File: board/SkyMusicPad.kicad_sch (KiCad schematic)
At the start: 36 parts, among them SW1 Cherry, SW10 Cherry, SW11 Cherry, SW12 Cherry, SW13 Cherry, SW14 Cherry, SW15 Cherry, SW16 RotaryEncoder_Switch, SW2 Cherry, SW3 Cherry, SW4 Cherry, SW5 Cherry, SW6 Cherry, SW7 Cherry, SW8 Cherry, SW9 Cherry

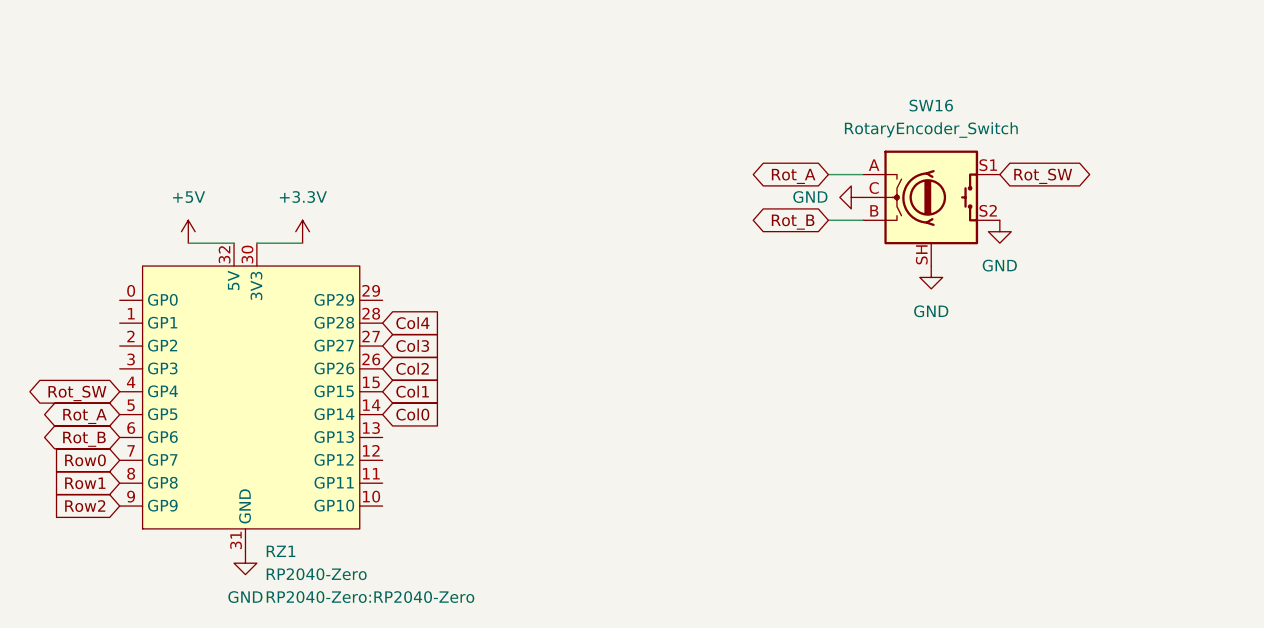
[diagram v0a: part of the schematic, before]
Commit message: Change global net shapes, move encoder position
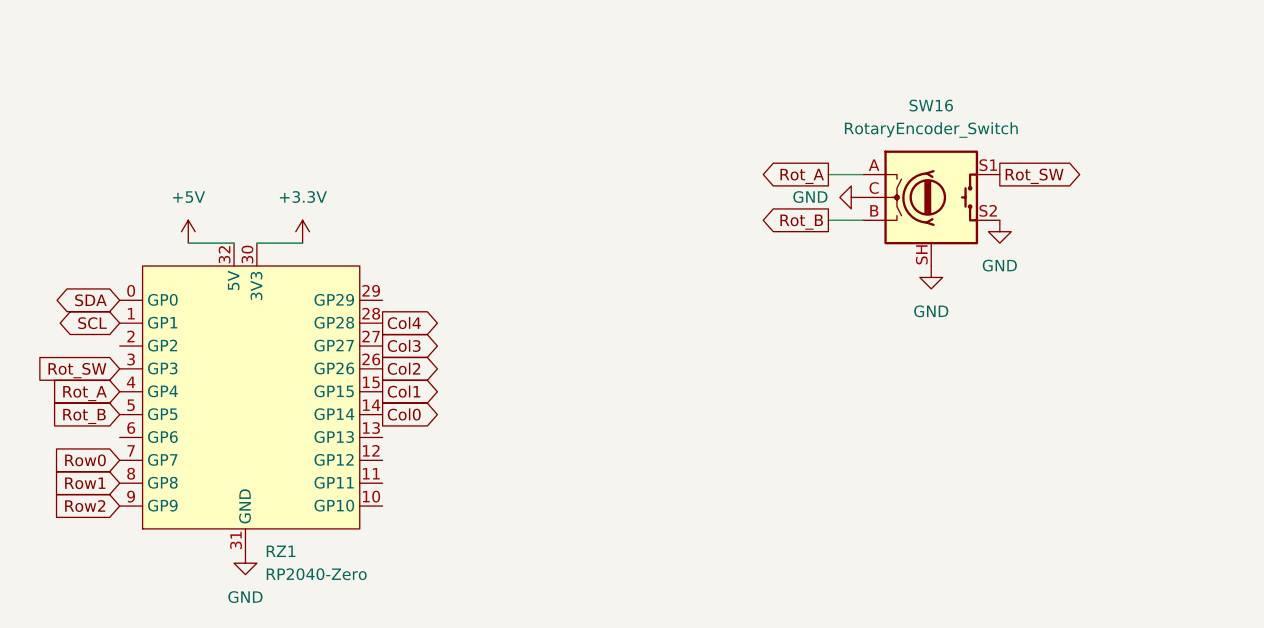
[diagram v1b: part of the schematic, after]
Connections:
- net Rot_A: now also RZ1.4 (GP4); no longer RZ1.5 (GP5)
- net Rot_B: now also RZ1.5 (GP5); no longer RZ1.6 (GP6)
- net Rot_SW: now also RZ1.3 (GP3); no longer RZ1.4 (GP4)
- net SDA: now reaches RZ1.0 (GP0)
- net SCL: now reaches RZ1.1 (GP1)
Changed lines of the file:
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@@
 (kicad_sch
-	(version 20240101)
+	(version 20231120)
 	(generator "eeschema")
-	(generator_version "8.99")
+	(generator_version "8.0")
 	(paper "A4")
 	(junction
@@
 		)
 	)
+	(global_label "SCL"
+		(shape bidirectional)
+		(at 52.07 133.35 180)
+		(fields_autoplaced yes)
+		(effects
+			(font
+				(size 1.27 1.27)
+			)
+			(justify right)
+		)
+		(property "Intersheetrefs" "${INTERSHEET_REFS}"
+			(at 44.4659 133.35 0)
+			(effects
+				(font
+					(size 1.27 1.27)
+				)
+				(justify right)
+				(hide yes)
+			)
+		)
+	)
 	(global_label "Row2"
 		(shape input)
@@
 	)
 	(global_label "Col1"
-		(shape input)
+		(shape output)
 		(at 81.28 140.97 0)
 		(fields_autoplaced yes)
@@
 	)
 	(global_label "Rot_A"
-		(shape bidirectional)
+		(shape output)
 		(at 130.81 116.84 180)
 		(fields_autoplaced yes)
@@
 		)
 		(property "Intersheetrefs" "${INTERSHEET_REFS}"
-			(at 121.5126 116.84 0)
+			(at 122.6239 116.84 0)
 			(effects
 				(font
@@
 	)
 	(global_label "Rot_B"
-		(shape bidirectional)
-		(at 52.07 146.05 180)
+		(shape input)
+		(at 52.07 143.51 180)
 		(fields_autoplaced yes)
 		(effects
@@
 		)
 		(property "Intersheetrefs" "${INTERSHEET_REFS}"
-			(at 42.5912 146.05 0)
+			(at 43.7025 143.51 0)
 			(effects
 				(font
@@
 	)
 	(global_label "Col2"
-		(shape input)
+		(shape output)
 		(at 81.28 138.43 0)
 		(fields_autoplaced yes)
@@
 	)
 	(global_label "Rot_SW"
-		(shape bidirectional)
-		(at 52.07 140.97 180)
+		(shape input)
+		(at 52.07 138.43 180)
 		(fields_autoplaced yes)
 		(effects
@@
 		)
 		(property "Intersheetrefs" "${INTERSHEET_REFS}"
-			(at 41.2003 140.97 0)
+			(at 42.3116 138.43 0)
 			(effects
 				(font
@@
 	)
 	(global_label "Col0"
-		(shape input)
+		(shape output)
 		(at 81.28 143.51 0)
 		(fields_autoplaced yes)
@@
 	)
 	(global_label "Rot_A"
-		(shape bidirectional)
-		(at 52.07 143.51 180)
+		(shape input)
+		(at 52.07 140.97 180)
 		(fields_autoplaced yes)
 		(effects
@@
 		)
 		(property "Intersheetrefs" "${INTERSHEET_REFS}"
-			(at 42.7726 143.51 0)
+			(at 43.8839 140.97 0)
 			(effects
 				(font
@@
 	)
 	(global_label "Col4"
-		(shape input)
+		(shape output)
 		(at 81.28 133.35 0)
 		(fields_autoplaced yes)
@@
 		)
 	)
+	(global_label "SDA"
+		(shape bidirectional)
+		(at 52.07 130.81 180)
+		(fields_autoplaced yes)
+		(effects
+			(font
+				(size 1.27 1.27)
+			)
+			(justify right)
+		)
+		(property "Intersheetrefs" "${INTERSHEET_REFS}"
+			(at 44.4054 130.81 0)
+			(effects
+				(font
+					(size 1.27 1.27)
+				)
+				(justify right)
+				(hide yes)
+			)
+		)
+	)
 	(global_label "Col1"
 		(shape input)
@@
 	)
 	(global_label "Col3"
-		(shape input)
+		(shape output)
 		(at 81.28 135.89 0)
 		(fields_autoplaced yes)
@@
 	)
 	(global_label "Rot_SW"
-		(shape bidirectional)
+		(shape output)
 		(at 149.86 116.84 0)
 		(fields_autoplaced yes)
@@
 		)
 		(property "Intersheetrefs" "${INTERSHEET_REFS}"
-			(at 160.7297 116.84 0)
+			(at 159.6184 116.84 0)
 			(effects
 				(font
@@
 	)
 	(global_label "Rot_B"
-		(shape bidirectional)
+		(shape output)
 		(at 130.81 121.92 180)
 		(fields_autoplaced yes)
@@
 		)
 		(property "Intersheetrefs" "${INTERSHEET_REFS}"
-			(at 121.3312 121.92 0)
+			(at 122.4425 121.92 0)
 			(effects
 				(font
@@
 				)
 				(justify left)
+				(hide yes)
 			)
 		)

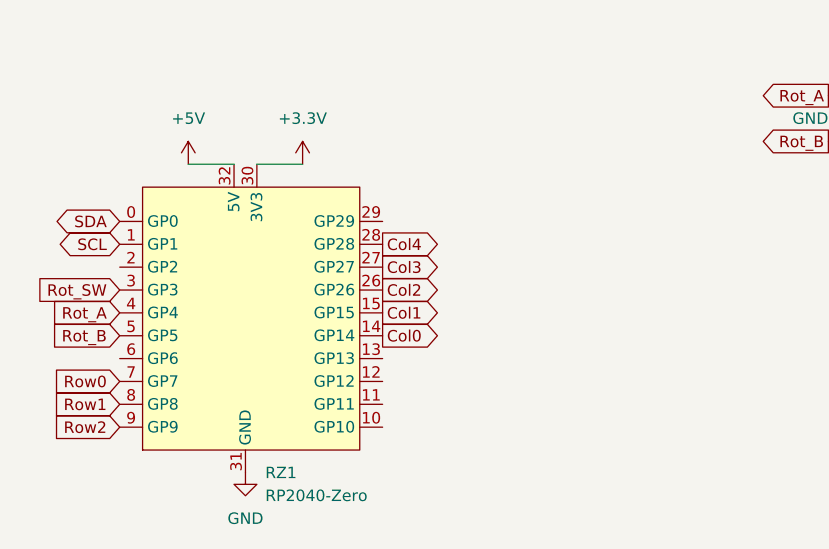
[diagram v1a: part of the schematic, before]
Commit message: Code migration
- Remove CircuitPython code
- Begin Arduino code development
- Add patched BLE Keyboard library
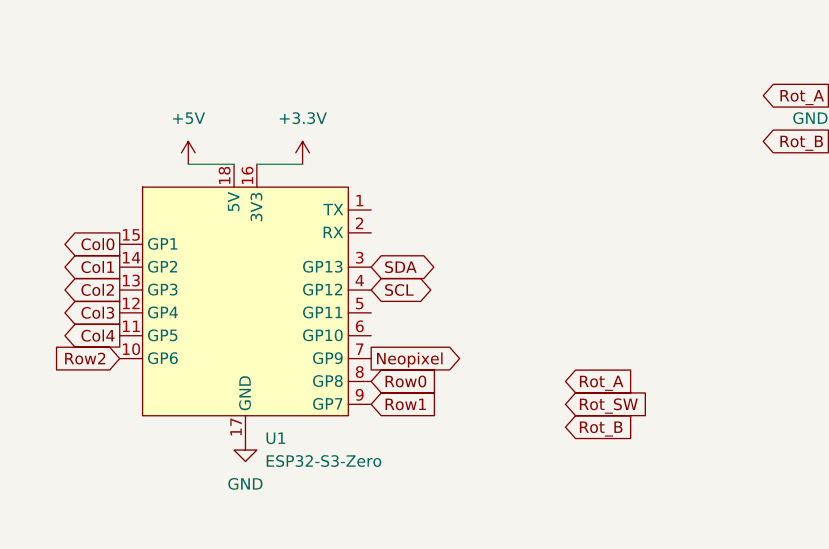
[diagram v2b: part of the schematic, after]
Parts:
- removed RZ1: RP2040-Zero, RP2040-Zero:RP2040-Zero, symbol rp2040-zero:RP2040-Zero
- added U1: ESP32-S3-Zero, ESP32-S3-Zero:ESP32-S3-Zero, symbol ESP32-S3-Zero:ESP32-S3-Zero
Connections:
- net +3.3V: now also U1.16 (3V3)
- net +5V: now also U1.18 (5V)
- net Col0: now also U1.15 (GP1)
- net Col1: now also U1.14 (GP2)
- net Col2: now also U1.13 (GP3)
- net Col3: now also U1.12 (GP4)
- net Col4: now also U1.11 (GP5)
- net GND: now also U1.17 (GND)
- net Row0: now also U1.8 (GP8)
- net Row1: now also U1.9 (GP7)
- net Row2: now also U1.10 (GP6)
- net SCL: now also U1.4 (GP12)
- net SDA: now also U1.3 (GP13)
- new net Neopixel: U1.7 (GP9)

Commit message: Code and PCB updates
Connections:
- net Rot_A: now also U1.5 (GP11)
- net Rot_B: now also U1.6 (GP10)
- net Rot_SW: now also U1.2 (RX)
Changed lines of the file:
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@@
 	(global_label "Rot_B"
 		(shape input)
-		(at 101.6 153.67 0)
-		(fields_autoplaced yes)
-		(effects
-			(font
-				(size 1.27 1.27)
-			)
-			(justify left)
-		)
-		(property "Intersheetrefs" "${INTERSHEET_REFS}"
-			(at 109.9675 153.67 0)
+		(at 80.01 143.51 0)
+		(fields_autoplaced yes)
+		(effects
+			(font
+				(size 1.27 1.27)
+			)
+			(justify left)
+		)
+		(property "Intersheetrefs" "${INTERSHEET_REFS}"
+			(at 88.3775 143.51 0)
 			(effects
 				(font
@@
 	(global_label "Rot_SW"
 		(shape input)
-		(at 101.6 151.13 0)
-		(fields_autoplaced yes)
-		(effects
-			(font
-				(size 1.27 1.27)
-			)
-			(justify left)
-		)
-		(property "Intersheetrefs" "${INTERSHEET_REFS}"
-			(at 111.3584 151.13 0)
+		(at 80.01 132.08 0)
+		(fields_autoplaced yes)
+		(effects
+			(font
+				(size 1.27 1.27)
+			)
+			(justify left)
+		)
+		(property "Intersheetrefs" "${INTERSHEET_REFS}"
+			(at 89.7684 132.08 0)
 			(effects
 				(font
@@
 	(global_label "Rot_A"
 		(shape input)
-		(at 101.6 148.59 0)
-		(fields_autoplaced yes)
-		(effects
-			(font
-				(size 1.27 1.27)
-			)
-			(justify left)
-		)
-		(property "Intersheetrefs" "${INTERSHEET_REFS}"
-			(at 109.7861 148.59 0)
-			(effects
-				(font
+		(at 80.01 140.97 0)
+		(fields_autoplaced yes)
+		(effects
+			(font
+				(size 1.27 1.27)
+			)
+			(justify left)
+		)
+		(property "Intersheetrefs" "${INTERSHEET_REFS}"
+			(at 88.1961 140.97 0)
+			(effects
+				(font

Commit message: Further board and code development.
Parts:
- added BT1: Battery_Cell, symbol Device:Battery_Cell
- added D16, D17, D18, D19, D20, D21, D22, D23, D24, D25, D26, D27, D28, D29, D30: WS2812B-2020, LED_SMD:LED_WS2812B-2020_PLCC4_2.0x2.0mm, symbol LED:WS2812B-2020
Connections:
- net +3.3V: now also D16.4 (VDD), D17.4 (VDD), D18.4 (VDD), D19.4 (VDD), D20.4 (VDD), D21.4 (VDD), D22.4 (VDD), D23.4 (VDD), D24.4 (VDD), D25.4 (VDD), D26.4 (VDD), D27.4 (VDD), D28.4 (VDD), D29.4 (VDD), D30.4 (VDD)
- net Col0: now also U1.11 (GP5); no longer U1.15 (GP1)
- net Col1: now also U1.12 (GP4); no longer U1.14 (GP2)
- net Col3: now also U1.14 (GP2); no longer U1.12 (GP4)
- net Col4: now also U1.15 (GP1); no longer U1.11 (GP5)
- net GND: now also BT1.2 (-), D16.2 (VSS), D17.2 (VSS), D18.2 (VSS), D19.2 (VSS), D20.2 (VSS), D21.2 (VSS), D22.2 (VSS), D23.2 (VSS), D24.2 (VSS), D25.2 (VSS), D26.2 (VSS), D27.2 (VSS), D28.2 (VSS), D29.2 (VSS), D30.2 (VSS)
- net Neopixel: now also D16.3 (DIN)
- net Batt: now reaches U1.1 (TX)
- net Batt: now also BT1.1 (+)
- new net: D16.1 (DOUT), D17.3 (DIN)
- new net: D27.1 (DOUT), D28.3 (DIN)
- new net: D26.1 (DOUT), D27.3 (DIN)
- new net: D18.1 (DOUT), D19.3 (DIN)
- new net: D17.1 (DOUT), D18.3 (DIN)
- new net: D22.1 (DOUT), D23.3 (DIN)
- new net: D21.1 (DOUT), D22.3 (DIN)
- new net: D29.1 (DOUT), D30.3 (DIN)
- new net: D24.1 (DOUT), D25.3 (DIN)
- new net: D23.1 (DOUT), D24.3 (DIN)
- new net: D28.1 (DOUT), D29.3 (DIN)
- new net: D19.1 (DOUT), D20.3 (DIN)
- new net Row0_out: D20.1 (DOUT), D21.3 (DIN)
- new net Row1_out: D25.1 (DOUT), D26.3 (DIN)

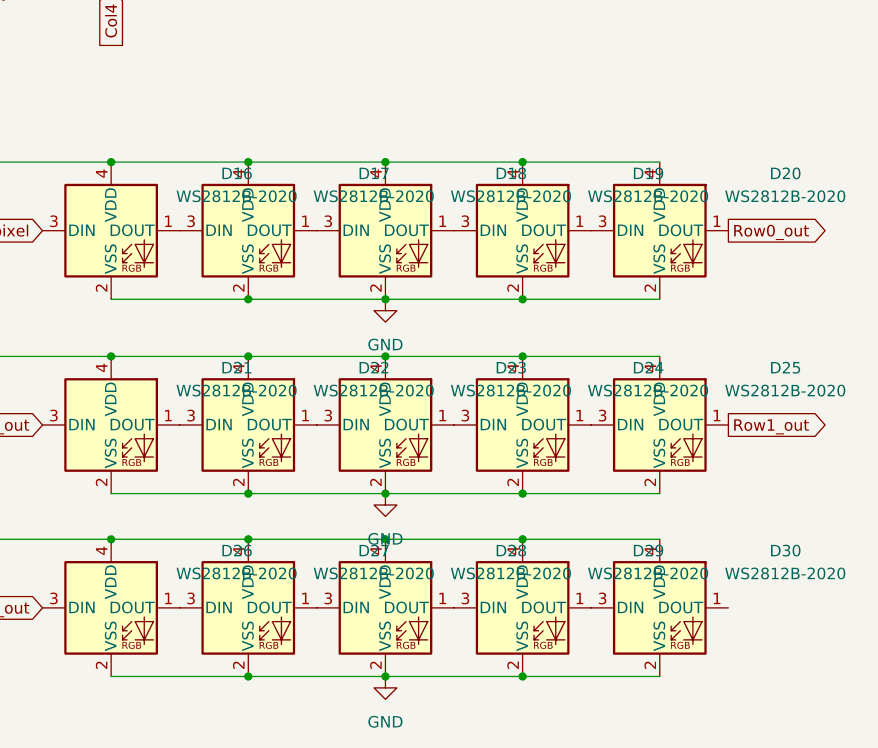
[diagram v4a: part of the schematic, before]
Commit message: Fix and add LEDs
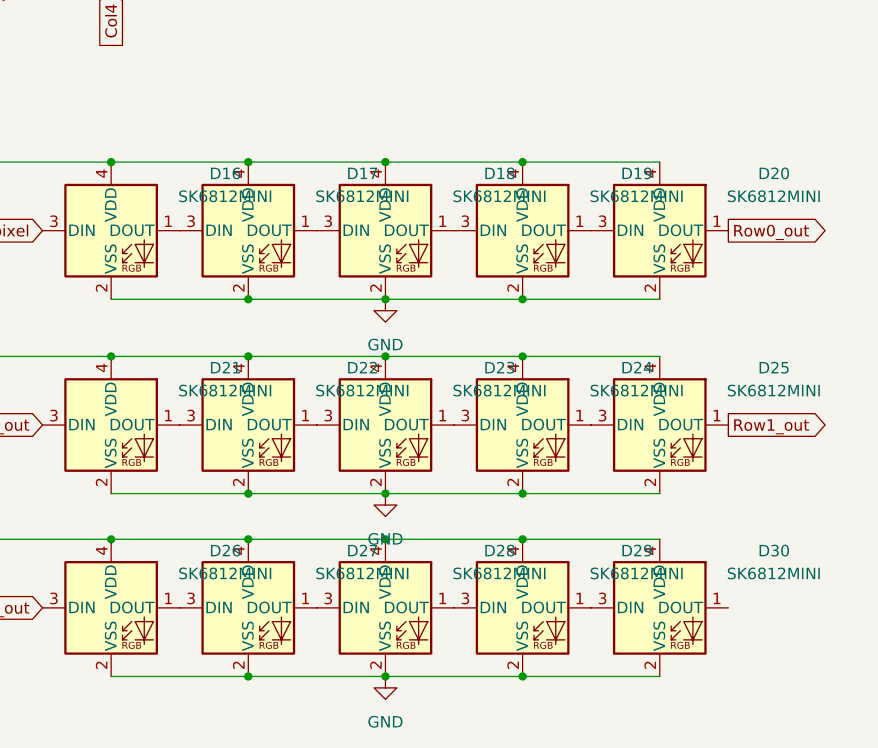
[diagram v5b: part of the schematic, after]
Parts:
- D16, D17, D18, D19, D20, D21, D22, D23, D24, D25, D26, D27, D28, D29, D30: value WS2812B-2020 -> SK6812MINI; footprint LED_SMD:LED_WS2812B-2020_PLCC4_2.0x2.0mm -> SkyKeypad:LED_SK6812MINI_REVERSE; symbol LED:WS2812B-2020 -> LED:SK6812MINI
